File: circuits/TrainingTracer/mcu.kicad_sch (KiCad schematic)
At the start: 2 parts, among them J8 NUCLEO-F303K8, J9 NUCLEO-F303K8

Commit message: 回路完成
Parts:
- J18: renamed from J8; footprint (none) -> Connector_PinSocket_2.54mm:PinSocket_1x15_P2.54mm_Vertical
- J19: renamed from J9; footprint (none) -> Connector_PinSocket_2.54mm:PinSocket_1x15_P2.54mm_Vertical
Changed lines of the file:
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@@
 		(dnp no)
 		(fields_autoplaced yes)
-		(property "Reference" "#PWR063"
+		(property "Reference" "#PWR067"
 			(at 153.67 73.66 0)
 			(effects
@@
 			(project ""
 				(path "/914faf3b-320c-40a9-bc45-7ad88109862b/5dce65b8-efc9-4083-92d8-69d373b0fd14"
-					(reference "#PWR063")
+					(reference "#PWR067")
 					(unit 1)
 				)
@@
 		(on_board yes)
 		(dnp no)
-		(property "Reference" "J8"
+		(property "Reference" "J18"
 			(at 105.918 65.786 0)
 			(effects
@@
 			)
 		)
-		(property "Footprint" ""
+		(property "Footprint" "Connector_PinSocket_2.54mm:PinSocket_1x15_P2.54mm_Vertical"
 			(at 109.22 88.9 0)
 			(effects
@@
 			(project ""
 				(path "/914faf3b-320c-40a9-bc45-7ad88109862b/5dce65b8-efc9-4083-92d8-69d373b0fd14"
-					(reference "J8")
+					(reference "J18")
 					(unit 1)
 				)
@@
 		(dnp no)
 		(fields_autoplaced yes)
-		(property "Reference" "#PWR064"
+		(property "Reference" "#PWR068"
 			(at 156.21 120.65 0)
 			(effects
@@
 			(project ""
 				(path "/914faf3b-320c-40a9-bc45-7ad88109862b/5dce65b8-efc9-4083-92d8-69d373b0fd14"
-					(reference "#PWR064")
+					(reference "#PWR068")
 					(unit 1)
 				)
@@
 		(dnp no)
 		(fields_autoplaced yes)
-		(property "Reference" "#PWR062"
+		(property "Reference" "#PWR066"
 			(at 100.33 120.65 0)
 			(effects
@@
 			(project ""
 				(path "/914faf3b-320c-40a9-bc45-7ad88109862b/5dce65b8-efc9-4083-92d8-69d373b0fd14"
-					(reference "#PWR062")
+					(reference "#PWR066")
 					(unit 1)
 				)
@@
 		(on_board yes)
 		(dnp no)
-		(property "Reference" "J9"
+		(property "Reference" "J19"
 			(at 148.082 65.786 0)
 			(effects
@@
 			)
 		)
-		(property "Footprint" ""
+		(property "Footprint" "Connector_PinSocket_2.54mm:PinSocket_1x15_P2.54mm_Vertical"
 			(at 144.78 88.9 0)
 			(effects
@@
 			(project "TrainingTracer"
 				(path "/914faf3b-320c-40a9-bc45-7ad88109862b/5dce65b8-efc9-4083-92d8-69d373b0fd14"
-					(reference "J9")
-					(unit 1)
-				)
+					(reference "J19")
+					(unit 1)
+				)

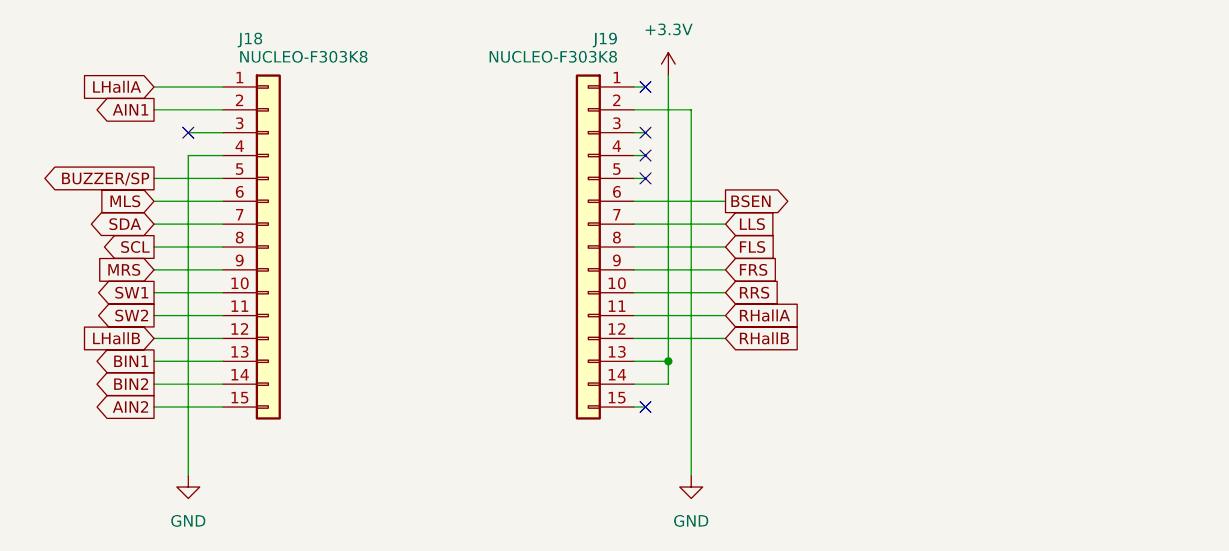
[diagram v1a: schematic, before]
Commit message: 改造箇所の漏れを追加 (+その他)
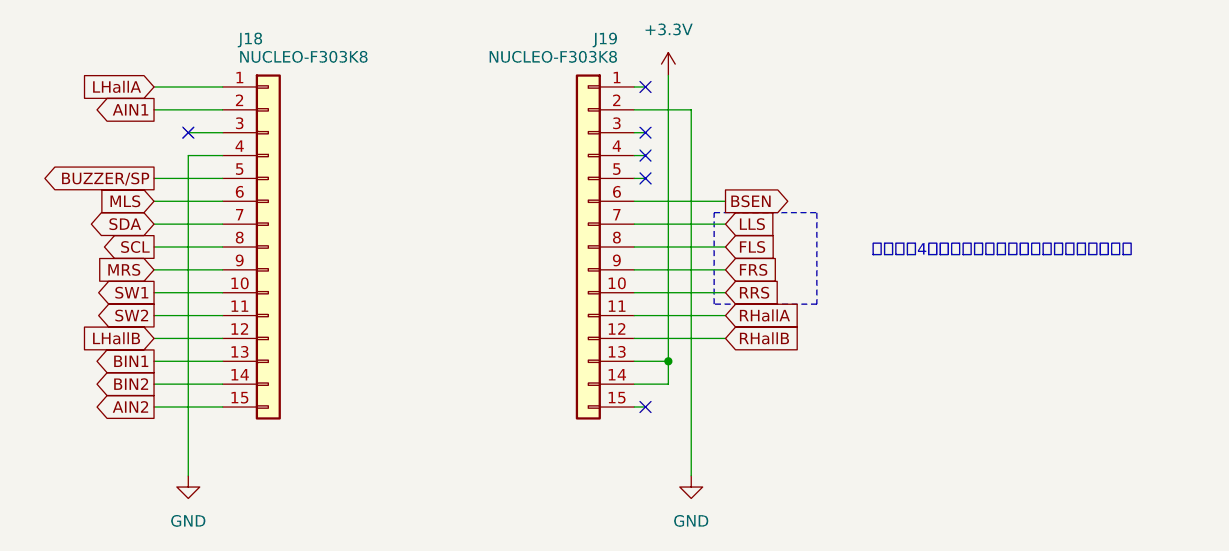
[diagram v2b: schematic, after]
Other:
- note added: "改良箇所4：ラベルの命名をソフト上の命名と統一"
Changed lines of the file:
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@@
 	(generator_version "9.0")
 	(paper "A4")
+	(rectangle
+		(start 158.75 85.09)
+		(end 170.18 95.25)
+		(stroke
+			(width 0)
+			(type dash_dot)
+		)
+		(fill
+			(type none)
+		)
+	)
+	(text "改良箇所4：ラベルの命名をソフト上の命名と統一"
+		(exclude_from_sim no)
+		(at 190.754 89.408 0)
+		(effects
+			(font
+				(size 1.27 1.27)
+			)
+		)
+	)
 	(junction
 		(at 153.67 101.6)
